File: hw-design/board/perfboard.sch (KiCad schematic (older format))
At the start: 13 parts, among them P10 Power, P11 Analog, P12 Digital, P13 Digital

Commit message: sch: changing input voltage from +9V to +12V
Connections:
- net +9V renamed +12V
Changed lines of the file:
@@
-$EndComp
-$Comp
-L +9V #PWR041
-U 1 1 558D5D1A
-P 1950 2350
-F 0 "#PWR041" H 1950 2200 50  0001 C CNN
-F 1 "+9V" H 1950 2490 50  0000 C CNN
-F 2 "" H 1950 2350 60  0000 C CNN
-F 3 "" H 1950 2350 60  0000 C CNN
-	1    1950 2350
-	1    0    0    -1
 $EndComp
 $Comp
@@
 NoConn ~ 3100 1450
 NoConn ~ 3100 1850
+$Comp
+L +12V #PWR?
+U 1 1 560B7619
+P 1950 2350
+F 0 "#PWR?" H 1950 2200 50  0001 C CNN
+F 1 "+12V" H 1950 2490 50  0000 C CNN
+F 2 "" H 1950 2350 60  0000 C CNN
+F 3 "" H 1950 2350 60  0000 C CNN
+	1    1950 2350
+	1    0    0    -1
+$EndComp
 $EndSCHEMATC

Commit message: fix all DRC issues
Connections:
- no-connect marks 107 -> 85
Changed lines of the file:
@@
 	1    0    0    -1
 $EndComp
-NoConn ~ 1750 1700
-NoConn ~ 1750 1800
-NoConn ~ 1750 2850
-NoConn ~ 1750 2950
-NoConn ~ 1750 3050
-NoConn ~ 1750 3150
-NoConn ~ 3100 3000
-NoConn ~ 3100 2900
-NoConn ~ 3100 2800
-NoConn ~ 3100 2700
-NoConn ~ 3100 2600
-NoConn ~ 3100 2350
-NoConn ~ 3100 2250
-NoConn ~ 3100 2150
-NoConn ~ 3100 2050
-NoConn ~ 3100 1950
-NoConn ~ 3100 1650
-$Comp
-L GNDD #PWR037
+$Comp
+L GNDD #PWR10
 U 1 1 558D5D07
 P 2550 1850
-F 0 "#PWR037" H 2550 1600 50  0001 C CNN
+F 0 "#PWR10" H 2550 1600 50  0001 C CNN
 F 1 "GNDD" H 2550 1700 50  0000 C CNN
 F 2 "" H 2550 1850 60  0000 C CNN
@@
 $EndComp
 $Comp
-L GNDD #PWR038
+L GNDD #PWR3
 U 1 1 558D5D0F
 P 2150 2250
-F 0 "#PWR038" H 2150 2000 50  0001 C CNN
+F 0 "#PWR3" H 2150 2000 50  0001 C CNN
 F 1 "GNDD" H 2150 2100 50  0000 C CNN
 F 2 "" H 2150 2250 60  0000 C CNN
@@
 $EndComp
 $Comp
-L +5V #PWR039
+L +5V #PWR7
 U 1 1 558D5D24
 P 2350 1950
-F 0 "#PWR039" H 2350 1800 50  0001 C CNN
+F 0 "#PWR7" H 2350 1800 50  0001 C CNN
 F 1 "+5V" H 2350 2090 50  0000 C CNN
 F 2 "" H 2350 1950 60  0000 C CNN
@@
 $EndComp
 $Comp
-L +3.3V #PWR040
+L +3.3V #PWR4
 U 1 1 558D5D2C
 P 2200 1850
-F 0 "#PWR040" H 2200 1700 50  0001 C CNN
+F 0 "#PWR4" H 2200 1700 50  0001 C CNN
 F 1 "+3.3V" H 2200 1990 50  0000 C CNN
 F 2 "" H 2200 1850 60  0000 C CNN
@@
 $EndComp
 $Comp
-L GNDD #PWR041
+L GNDD #PWR33
 U 1 1 558D7D87
 P 8600 2950
-F 0 "#PWR041" H 8600 2700 50  0001 C CNN
+F 0 "#PWR33" H 8600 2700 50  0001 C CNN
 F 1 "GNDD" H 8600 2800 50  0000 C CNN
 F 2 "" H 8600 2950 60  0000 C CNN
@@
 $EndComp
 $Comp
-L +5V #PWR042
+L +5V #PWR31
 U 1 1 558D90B9
 P 8150 1450
-F 0 "#PWR042" H 8150 1300 50  0001 C CNN
+F 0 "#PWR31" H 8150 1300 50  0001 C CNN
 F 1 "+5V" H 8150 1590 50  0000 C CNN
 F 2 "" H 8150 1450 60  0000 C CNN
@@
 $EndComp
 $Comp
-L +3.3V #PWR043
+L +3.3V #PWR29
 U 1 1 558D93C3
 P 7700 1450
-F 0 "#PWR043" H 7700 1300 50  0001 C CNN
+F 0 "#PWR29" H 7700 1300 50  0001 C CNN
 F 1 "+3.3V" H 7700 1590 50  0000 C CNN
 F 2 "" H 7700 1450 60  0000 C CNN
@@
 	8200 1550 8150 1550
 Connection ~ 8150 1550
-NoConn ~ 1750 2750
-NoConn ~ 1750 2650
-NoConn ~ 3100 1550
-NoConn ~ 3100 1450
-NoConn ~ 3100 1850
-$Comp
-L +12V #PWR044
+$Comp
+L +12V #PWR2
 U 1 1 560B7619
 P 1950 2350
-F 0 "#PWR044" H 1950 2200 50  0001 C CNN
+F 0 "#PWR2" H 1950 2200 50  0001 C CNN
 F 1 "+12V" H 1950 2490 50  0000 C CNN
 F 2 "" H 1950 2350 60  0000 C CNN

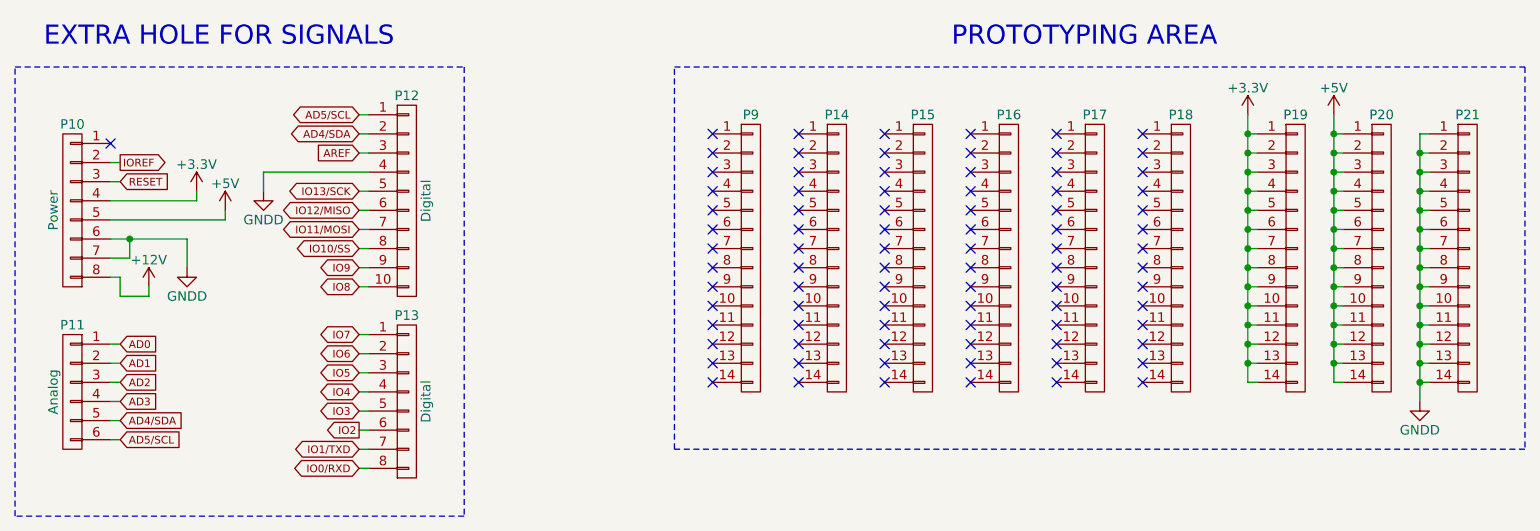
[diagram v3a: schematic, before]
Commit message: replace multiple headers by perfboard
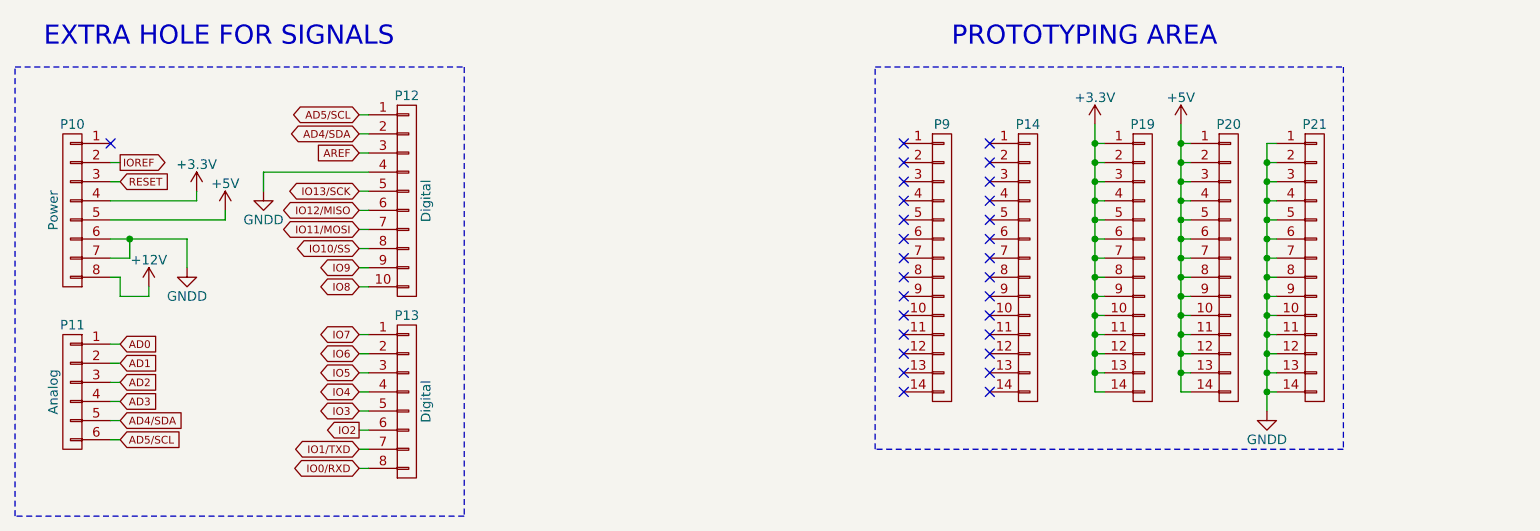
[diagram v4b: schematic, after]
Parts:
- removed P15, P16, P17, P18: ~, Pin_Headers:Pin_Header_Straight_1x14, symbol CONN_01X14
- P14, P9: footprint Pin_Headers:Pin_Header_Straight_1x14 -> Socket_Arduino_Uno:Perfboard
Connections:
- no-connect marks 85 -> 29
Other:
- moved on the sheet: P14, P19, P20, P21, P9

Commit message: fix pin name (vin)
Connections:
- net +12V renamed VIN
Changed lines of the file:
@@
 	1750 2300 1800 2300
-Wire Wire Line
-	1800 2300 1800 2400
-Wire Wire Line
-	1800 2400 1950 2400
-Wire Wire Line
-	1950 2400 1950 2350
 Wire Wire Line
 	1750 2000 2350 2000
@@
 	7400 1600 7350 1600
 Connection ~ 7350 1600
-$Comp
-L +12V #PWR2
-U 1 1 560B7619
-P 1950 2350
-F 0 "#PWR2" H 1950 2200 50  0001 C CNN
-F 1 "+12V" H 1950 2490 50  0000 C CNN
-F 2 "" H 1950 2350 60  0000 C CNN
-F 3 "" H 1950 2350 60  0000 C CNN
-	1    1950 2350
-	1    0    0    -1
-$EndComp
+Text GLabel 1800 2300 2    40   Input ~ 0
+VIN
 $EndSCHEMATC
